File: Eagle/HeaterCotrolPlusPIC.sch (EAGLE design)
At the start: 35 parts, among them Q1 P-FET

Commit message: Update HeaterCotrolPlusPIC.sch
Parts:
- added R9: 10K, SparkFun-Resistors:RESISTOR0805-RES
- R6: value 10K -> 4K7
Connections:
- net 3V3: now also R9.2
- net IO14: now also R6.2, U$10.P$1; no longer LEFT.P3
- net IO16: now also LEFT.P3, R9.1; no longer R6.2, U$10.P$1
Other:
- note removed: "Not used"
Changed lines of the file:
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@@
 <part name="-" library="wirepad" deviceset="1,6/0,8" device=""/>
 <part name="D1" library="SparkFun-DiscreteSemi" deviceset="DIODE" device="BAS16" value="250mA/100V"/>
-<part name="R6" library="SparkFun-Resistors" deviceset="RESISTOR" device="0805-RES" value="10K"/>
+<part name="R6" library="SparkFun-Resistors" deviceset="RESISTOR" device="0805-RES" value="4K7"/>
 <part name="U$8" library="CuriousTech" deviceset="SMD-PAD1" device=""/>
 <part name="10F320" library="Microchip_By_element14_Batch_1" deviceset="PIC10F220T-I/OT" device="" value="PIC10F320T-I/OT"/>
@@
 <part name="C2" library="SparkFun-Capacitors" deviceset="CAP" device="" value="0.1uF"/>
 <part name="C3" library="SparkFun-Capacitors" deviceset="CAP" device="" value="0.1uF"/>
+<part name="R9" library="SparkFun-Resistors" deviceset="RESISTOR" device="0805-RES" value="10K"/>
 </parts>
 <sheets>
@@
 <wire x1="233.68" y1="190.5" x2="180.34" y2="190.5" width="0" layer="97" style="shortdash"/>
 <text x="203.2" y="185.42" size="2.1844" layer="97" font="vector">Buzzer</text>
-<text x="35.56" y="170.18" size="2.1844" layer="97">Not used</text>
 <wire x1="233.68" y1="190.5" x2="266.7" y2="190.5" width="0" layer="97" style="shortdash"/>
 <wire x1="266.7" y1="190.5" x2="266.7" y2="134.62" width="0" layer="97" style="shortdash"/>
@@
 <instance part="C2" gate="G$1" x="33.02" y="78.74" rot="MR0"/>
 <instance part="C3" gate="G$1" x="40.64" y="78.74" rot="MR0"/>
+<instance part="R9" gate="G$1" x="88.9" y="109.22" rot="R90"/>
 </instances>
 <busses>
@@
 <wire x1="99.06" y1="124.46" x2="99.06" y2="127" width="0.1524" layer="91"/>
 <wire x1="99.06" y1="127" x2="93.98" y2="127" width="0.1524" layer="91"/>
-<wire x1="93.98" y1="127" x2="86.36" y2="127" width="0.1524" layer="91"/>
+<wire x1="93.98" y1="127" x2="88.9" y2="127" width="0.1524" layer="91"/>
 <junction x="93.98" y="127"/>
+<pinref part="R9" gate="G$1" pin="2"/>
+<wire x1="88.9" y1="127" x2="86.36" y2="127" width="0.1524" layer="91"/>
+<wire x1="88.9" y1="114.3" x2="88.9" y2="127" width="0.1524" layer="91"/>
+<junction x="88.9" y="127"/>
 </segment>
 <segment>
@@
 </segment>
 <segment>
-<pinref part="LEFT" gate="G$1" pin="P3"/>
-<wire x1="73.66" y1="177.8" x2="73.66" y2="180.34" width="0.1524" layer="91"/>
-<label x="73.66" y="180.34" size="1.778" layer="95" rot="R90" xref="yes"/>
-</segment>
-</net>
-<net name="IO13" class="0">
-<segment>
-<pinref part="U$1" gate="G$1" pin="P$10"/>
-<wire x1="111.76" y1="81.28" x2="99.06" y2="81.28" width="0.1524" layer="91"/>
-<label x="99.06" y="81.28" size="1.778" layer="95" rot="R180" xref="yes"/>
-</segment>
-<segment>
-<pinref part="RIGHT" gate="G$1" pin="P1"/>
-<wire x1="109.22" y1="177.8" x2="109.22" y2="180.34" width="0.1524" layer="91"/>
-<label x="109.22" y="180.34" size="1.778" layer="95" rot="R90" xref="yes"/>
-</segment>
-</net>
-<net name="IO16" class="0">
-<segment>
-<wire x1="111.76" y1="96.52" x2="86.36" y2="96.52" width="0.1524" layer="91"/>
-<pinref part="U$1" gate="G$1" pin="P$13"/>
-<label x="86.36" y="96.52" size="1.778" layer="95" rot="R180" xref="yes"/>
-</segment>
-<segment>
 <wire x1="22.86" y1="180.34" x2="30.48" y2="180.34" width="0.1524" layer="91"/>
 <label x="35.56" y="180.34" size="1.778" layer="95" xref="yes"/>
@@
 </segment>
 </net>
+<net name="IO13" class="0">
+<segment>
+<pinref part="U$1" gate="G$1" pin="P$10"/>
+<wire x1="111.76" y1="81.28" x2="99.06" y2="81.28" width="0.1524" layer="91"/>
+<label x="99.06" y="81.28" size="1.778" layer="95" rot="R180" xref="yes"/>
+</segment>
+<segment>
+<pinref part="RIGHT" gate="G$1" pin="P1"/>
+<wire x1="109.22" y1="177.8" x2="109.22" y2="180.34" width="0.1524" layer="91"/>
+<label x="109.22" y="180.34" size="1.778" layer="95" rot="R90" xref="yes"/>
+</segment>
+</net>
+<net name="IO16" class="0">
+<segment>
+<wire x1="111.76" y1="96.52" x2="88.9" y2="96.52" width="0.1524" layer="91"/>
+<pinref part="U$1" gate="G$1" pin="P$13"/>
+<label x="81.28" y="96.52" size="1.778" layer="95" rot="R180" xref="yes"/>
+<pinref part="R9" gate="G$1" pin="1"/>
+<wire x1="88.9" y1="96.52" x2="81.28" y2="96.52" width="0.1524" layer="91"/>
+<wire x1="88.9" y1="104.14" x2="88.9" y2="96.52" width="0.1524" layer="91"/>
+<junction x="88.9" y="96.52"/>
+</segment>
+<segment>
+<pinref part="LEFT" gate="G$1" pin="P3"/>
+<wire x1="73.66" y1="177.8" x2="73.66" y2="180.34" width="0.1524" layer="91"/>
+<label x="73.66" y="180.34" size="1.778" layer="95" rot="R90" xref="yes"/>
+</segment>
+</net>

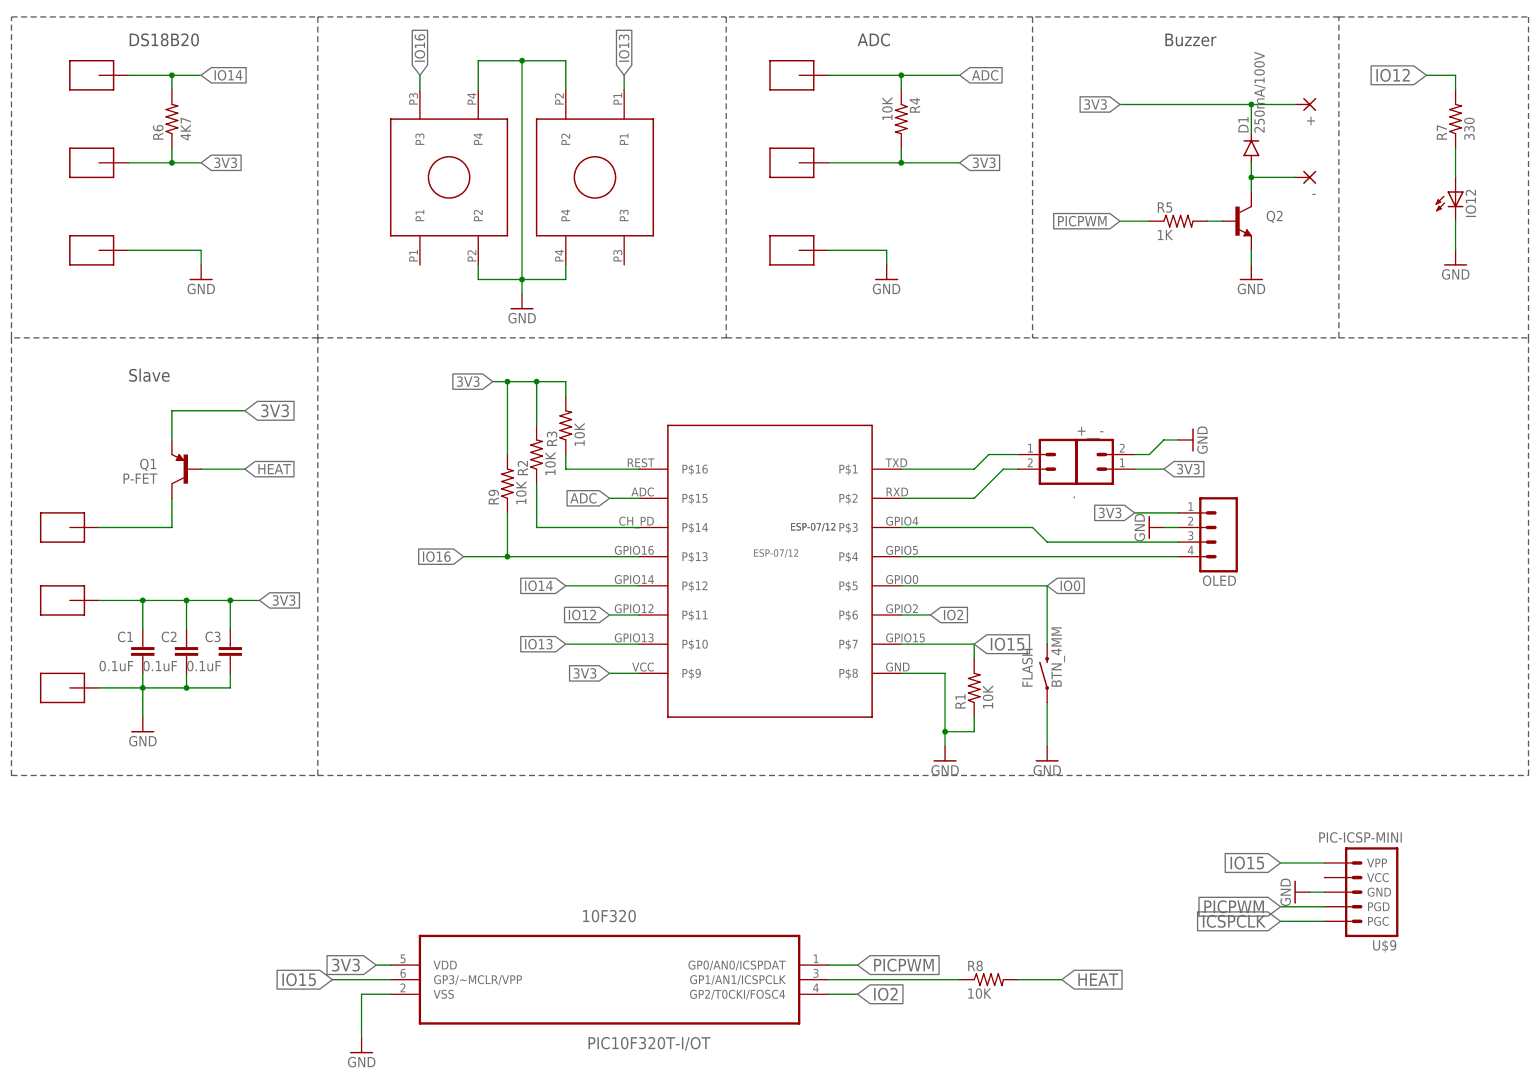
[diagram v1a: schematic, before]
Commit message: Added jumper for auto-reset
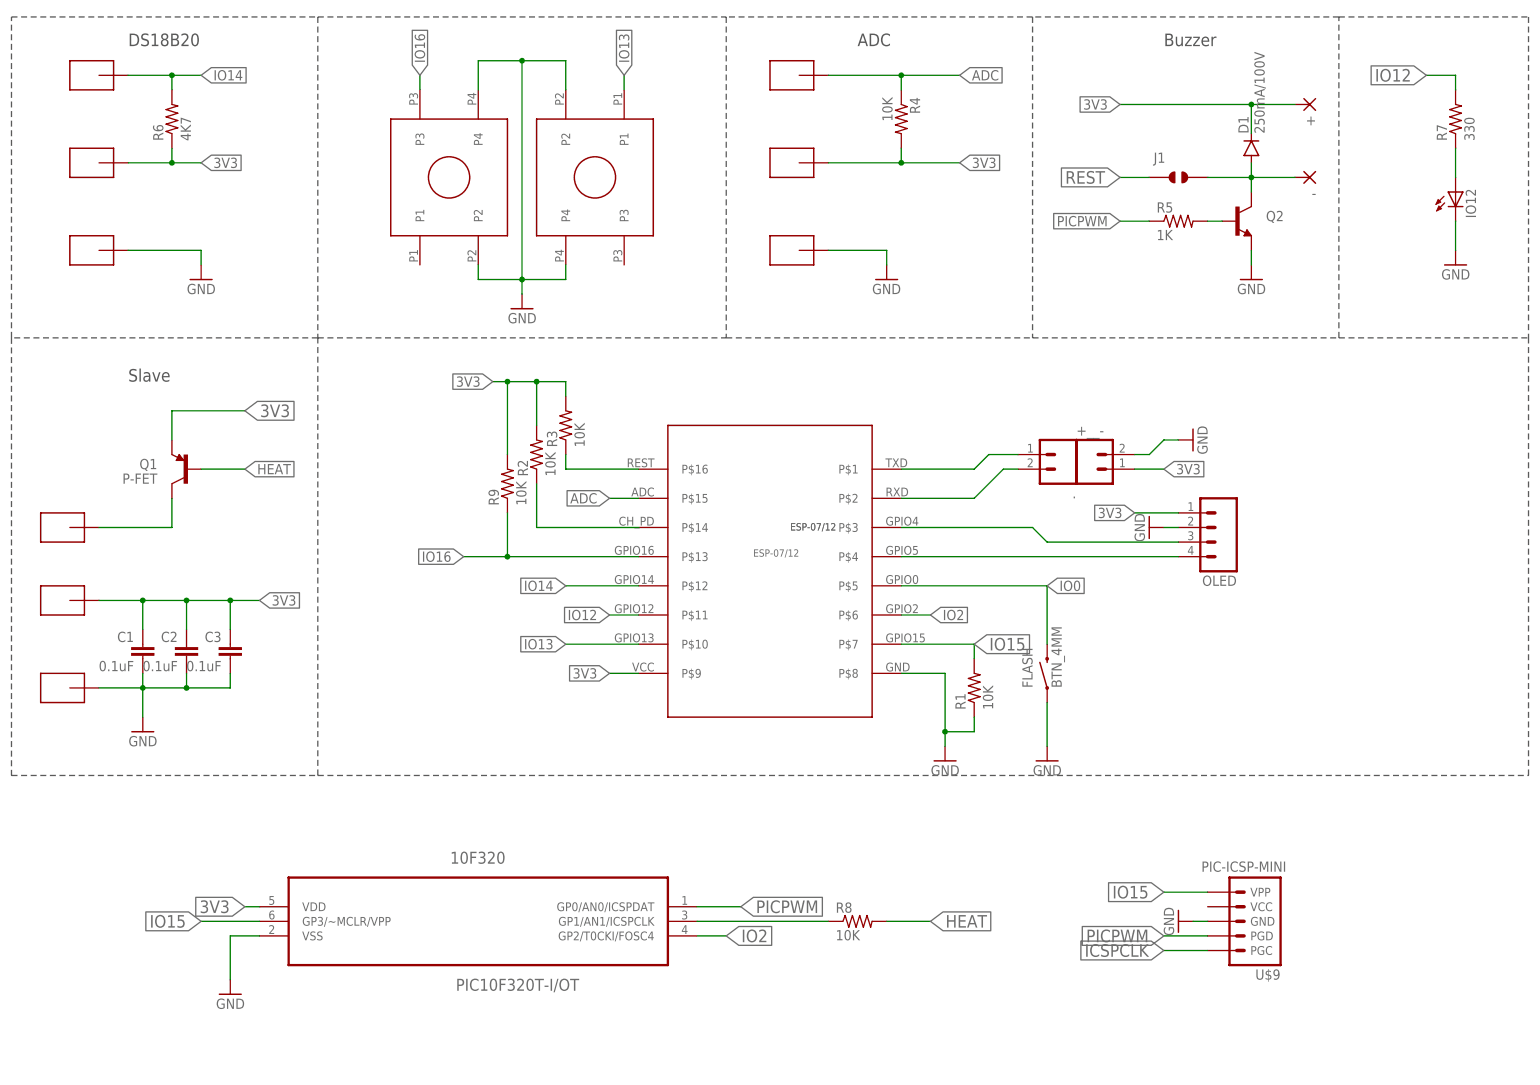
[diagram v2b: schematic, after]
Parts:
- added J1: JUMPER_SOLDER_1X2, dp_devices:JUMPER_SOLDER_1X2
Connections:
- removed net N$22: R3.1, U$1.P$16
- new net REST: J1.1, R3.1, U$1.P$16
- net N$4: now also J1.2
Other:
- moved on the sheet: 10F320, R8, U$9
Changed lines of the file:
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@@
 <?xml version="1.0" encoding="utf-8"?>
 <!DOCTYPE eagle SYSTEM "eagle.dtd">
-<eagle version="7.4.0">
+<eagle version="7.5.0">
 <drawing>
 <settings>
@@
 <part name="C3" library="SparkFun-Capacitors" deviceset="CAP" device="" value="0.1uF"/>
 <part name="R9" library="SparkFun-Resistors" deviceset="RESISTOR" device="0805-RES" value="10K"/>
+<part name="J1" library="dp_devices" deviceset="JUMPER_SOLDER_1X2" device=""/>
 </parts>
 <sheets>
@@
 <instance part="R6" gate="G$1" x="30.48" y="172.72" rot="R90"/>
 <instance part="U$8" gate="G$1" x="139.7" y="165.1" rot="R180"/>
-<instance part="10F320" gate="A" x="106.68" y="25.4"/>
+<instance part="10F320" gate="A" x="83.82" y="35.56"/>
 <instance part="IO12" gate="G$1" x="254" y="160.02"/>
 <instance part="R7" gate="G$1" x="254" y="172.72" rot="R90"/>
 <instance part="GND9" gate="1" x="254" y="147.32" rot="MR0"/>
-<instance part="R8" gate="G$1" x="172.72" y="22.86"/>
-<instance part="U$9" gate="G$1" x="238.76" y="38.1"/>
-<instance part="GND11" gate="1" x="63.5" y="10.16" rot="MR0"/>
-<instance part="GND12" gate="1" x="226.06" y="38.1" rot="MR90"/>
+<instance part="R8" gate="G$1" x="149.86" y="33.02"/>
+<instance part="U$9" gate="G$1" x="218.44" y="33.02"/>
+<instance part="GND11" gate="1" x="40.64" y="20.32" rot="MR0"/>
+<instance part="GND12" gate="1" x="205.74" y="33.02" rot="MR90"/>
 <instance part="C2" gate="G$1" x="33.02" y="78.74" rot="MR0"/>
 <instance part="C3" gate="G$1" x="40.64" y="78.74" rot="MR0"/>
 <instance part="R9" gate="G$1" x="88.9" y="109.22" rot="R90"/>
+<instance part="J1" gate="J" x="205.74" y="162.56"/>
 </instances>
 <busses>
@@
 <segment>
 <pinref part="10F320" gate="A" pin="GP3/~MCLR/VPP"/>
-<wire x1="58.42" y1="22.86" x2="68.58" y2="22.86" width="0.1524" layer="91"/>
-<label x="58.42" y="22.86" size="2.1844" layer="95" rot="R180" xref="yes"/>
+<wire x1="35.56" y1="33.02" x2="45.72" y2="33.02" width="0.1524" layer="91"/>
+<label x="35.56" y="33.02" size="2.1844" layer="95" rot="R180" xref="yes"/>
 </segment>
 <segment>
 <pinref part="U$9" gate="G$1" pin="VPP"/>
-<wire x1="231.14" y1="43.18" x2="223.52" y2="43.18" width="0.1524" layer="91"/>
-<label x="223.52" y="43.18" size="2.1844" layer="95" rot="R180" xref="yes"/>
+<wire x1="210.82" y1="38.1" x2="203.2" y2="38.1" width="0.1524" layer="91"/>
+<label x="203.2" y="38.1" size="2.1844" layer="95" rot="R180" xref="yes"/>
 </segment>
 </net>
@@
 <segment>
 <pinref part="10F320" gate="A" pin="VDD"/>
-<wire x1="66.04" y1="25.4" x2="68.58" y2="25.4" width="0.1524" layer="91"/>
-<label x="66.04" y="25.4" size="2.1844" layer="95" rot="R180" xref="yes"/>
+<wire x1="43.18" y1="35.56" x2="45.72" y2="35.56" width="0.1524" layer="91"/>
+<label x="43.18" y="35.56" size="2.1844" layer="95" rot="R180" xref="yes"/>
 </segment>
 </net>
@@
 </segment>
 <segment>
-<wire x1="63.5" y1="12.7" x2="63.5" y2="20.32" width="0.1524" layer="91"/>
+<wire x1="40.64" y1="22.86" x2="40.64" y2="30.48" width="0.1524" layer="91"/>
 <pinref part="10F320" gate="A" pin="VSS"/>
-<wire x1="68.58" y1="20.32" x2="63.5" y2="20.32" width="0.1524" layer="91"/>
+<wire x1="45.72" y1="30.48" x2="40.64" y2="30.48" width="0.1524" layer="91"/>
 <pinref part="GND11" gate="1" pin="GND"/>
 </segment>
@@
 <pinref part="U$9" gate="G$1" pin="GND"/>
 <pinref part="GND12" gate="1" pin="GND"/>
-<wire x1="231.14" y1="38.1" x2="228.6" y2="38.1" width="0.1524" layer="91"/>
-</segment>
-</net>
-<net name="N$22" class="0">
+<wire x1="210.82" y1="33.02" x2="208.28" y2="33.02" width="0.1524" layer="91"/>
+</segment>
+</net>
+<net name="REST" class="0">
 <segment>
 <wire x1="111.76" y1="111.76" x2="99.06" y2="111.76" width="0.1524" layer="91"/>
@@
 <wire x1="99.06" y1="114.3" x2="99.06" y2="111.76" width="0.1524" layer="91"/>
 <pinref part="U$1" gate="G$1" pin="P$16"/>
+</segment>
+<segment>
+<pinref part="J1" gate="J" pin="1"/>
+<wire x1="200.66" y1="162.56" x2="195.58" y2="162.56" width="0.1524" layer="91"/>
+<label x="195.58" y="162.56" size="2.1844" layer="95" rot="R180" xref="yes"/>
 </segment>
 </net>
@@
 <segment>
 <pinref part="10F320" gate="A" pin="GP2/T0CKI/FOSC4"/>
-<wire x1="149.86" y1="20.32" x2="144.78" y2="20.32" width="0.1524" layer="91"/>
-<label x="149.86" y="20.32" size="2.1844" layer="95" xref="yes"/>
+<wire x1="127" y1="30.48" x2="121.92" y2="30.48" width="0.1524" layer="91"/>
+<label x="127" y="30.48" size="2.1844" layer="95" xref="yes"/>
 </segment>
 </net>
@@
 <wire x1="218.44" y1="165.1" x2="218.44" y2="162.56" width="0.1524" layer="91"/>
 <junction x="218.44" y="162.56"/>
+<pinref part="J1" gate="J" pin="2"/>
+<wire x1="210.82" y1="162.56" x2="218.44" y2="162.56" width="0.1524" layer="91"/>
 </segment>
 </net>
@@
 <segment>
 <pinref part="10F320" gate="A" pin="GP0/AN0/ICSPDAT"/>
-<wire x1="144.78" y1="25.4" x2="149.86" y2="25.4" width="0.1524" layer="91"/>
-<label x="149.86" y="25.4" size="2.1844" layer="95" xref="yes"/>
+<wire x1="121.92" y1="35.56" x2="129.54" y2="35.56" width="0.1524" layer="91"/>
+<label x="129.54" y="35.56" size="2.1844" layer="95" xref="yes"/>
 </segment>
 <segment>
 <pinref part="U$9" gate="G$1" pin="PGD"/>
-<wire x1="231.14" y1="35.56" x2="223.52" y2="35.56" width="0.1524" layer="91"/>
-<label x="223.52" y="35.56" size="2.1844" layer="95" rot="R180" xref="yes"/>
+<wire x1="210.82" y1="30.48" x2="203.2" y2="30.48" width="0.1524" layer="91"/>
+<label x="203.2" y="30.48" size="2.1844" layer="95" rot="R180" xref="yes"/>
 </segment>
 </net>
@@
 <segment>
 <pinref part="10F320" gate="A" pin="GP1/AN1/ICSPCLK"/>
-<wire x1="167.64" y1="22.86" x2="144.78" y2="22.86" width="0.1524" layer="91"/>
+<wire x1="144.78" y1="33.02" x2="121.92" y2="33.02" width="0.1524" layer="91"/>
 <pinref part="R8" gate="G$1" pin="1"/>
 </segment>
 <segment>
 <pinref part="U$9" gate="G$1" pin="PGC"/>
-<wire x1="231.14" y1="33.02" x2="223.52" y2="33.02" width="0.1524" layer="91"/>
-<label x="223.52" y="33.02" size="2.1844" layer="95" rot="R180" xref="yes"/>
+<wire x1="210.82" y1="27.94" x2="203.2" y2="27.94" width="0.1524" layer="91"/>
+<label x="203.2" y="27.94" size="2.1844" layer="95" rot="R180" xref="yes"/>
 </segment>
 </net>
@@
 <segment>
 <pinref part="R8" gate="G$1" pin="2"/>
-<wire x1="177.8" y1="22.86" x2="185.42" y2="22.86" width="0.1524" layer="91"/>
-<label x="185.42" y="22.86" size="2.1844" layer="95" xref="yes"/>
-</segment>
-<segment>
+<wire x1="154.94" y1="33.02" x2="162.56" y2="33.02" width="0.1524" layer="91"/>
+<label x="162.56" y="33.02" size="2.1844" layer="95" xref="yes"/>
+</segment>
+<segment>
